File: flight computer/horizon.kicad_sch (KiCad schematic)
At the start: 37 parts, among them J2 Conn_02x03_Counter_Clockwise, J7 Conn_02x03_Counter_Clockwise, J8 Conn_02x03_Counter_Clockwise, U1 MMCU, U3 NMCU, U4 TMCU, Y1 Crystal

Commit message: Ummm, more baro routing to the MCU and stuff
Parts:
- removed R28: R, Resistor_SMD:R_0603_1608Metric, symbol Device:R
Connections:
- net SCK TMCU: now reaches U4.18 (PA09)
- net CS TMCU: no longer names the net of U4.17 (PA08)
- no-connect marks 82 -> 81
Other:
- note added: "Pull low to talk"
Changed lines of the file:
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@@
 		)
 	)
+	(text "Pull low to talk"
+		(exclude_from_sim no)
+		(at 187.706 49.784 0)
+		(effects
+			(font
+				(size 1.27 1.27)
+			)
+		)
+	)
 	(text "GPS → MCU RX"
 		(exclude_from_sim no)
@@
 	)
 	(junction
-		(at 176.53 49.53)
-		(diameter 0)
-		(color 0 0 0 0)
-	)
-	(junction
 		(at 52.07 30.48)
 		(diameter 0)
@@
 	)
 	(no_connect
-		(at 127 67.31)
-	)
-	(no_connect
 		(at 31.75 86.36)
 	)
@@
 	(wire
 		(pts
-			(xy 176.53 49.53) (xy 162.56 49.53)
-		)
-		(stroke
-			(width 0)
-			(type default)
-		)
-	)
-	(wire
-		(pts
 			(xy 46.99 31.75) (xy 52.07 31.75)
 		)
@@
 	(wire
 		(pts
-			(xy 177.8 49.53) (xy 176.53 49.53)
-		)
-		(stroke
-			(width 0)
-			(type default)
-		)
-	)
-	(wire
-		(pts
 			(xy 147.32 35.56) (xy 147.32 36.83)
 		)
@@
 	(global_label "CS_BARO TMCU"
 		(shape input)
-		(at 177.8 49.53 0)
+		(at 162.56 49.53 0)
 		(fields_autoplaced yes)
 		(effects
@@
 		)
 		(property "Intersheetrefs" "${INTERSHEET_REFS}"
-			(at 195.1785 49.53 0)
+			(at 179.9385 49.53 0)
 			(effects
 				(font
@@
 		)
 	)
+	(global_label "SCK TMCU"
+		(shape input)
+		(at 127 67.31 180)
+		(fields_autoplaced yes)
+		(effects
+			(font
+				(size 1.27 1.27)
+			)
+			(justify right)
+		)
+		(property "Intersheetrefs" "${INTERSHEET_REFS}"
+			(at 114.2782 67.31 0)
+			(effects
+				(font
+					(size 1.27 1.27)
+				)
+				(justify right)
+				(hide yes)
+			)
+		)
+	)
 	(global_label "TX TMCU"
 		(shape input)
@@
 		)
 	)
-	(global_label "CS TMCU"
-		(shape input)
-		(at 127 64.77 180)
-		(fields_autoplaced yes)
-		(effects
-			(font
-				(size 1.27 1.27)
-			)
-			(justify right)
-		)
-		(property "Intersheetrefs" "${INTERSHEET_REFS}"
-			(at 115.5482 64.77 0)
-			(effects
-				(font
-					(size 1.27 1.27)
-				)
-				(justify right)
-				(hide yes)
-			)
-		)
-	)
 	(global_label "I2C0_SDA"
 		(shape input)
@@
 	)
 	(symbol
-		(lib_id "Device:R")
-		(at 176.53 53.34 0)
-		(unit 1)
-		(exclude_from_sim no)
-		(in_bom yes)
-		(on_board yes)
-		(dnp no)
-		(property "Reference" "R28"
-			(at 171.196 53.594 0)
-			(effects
-				(font
-					(size 1.27 1.27)
-				)
-				(justify left)
-			)
-		)
-		(property "Value" "R"
-			(at 171.196 56.134 0)
-			(effects
-				(font
-					(size 1.27 1.27)
-				)
-				(justify left)
-			)
-		)
-		(property "Footprint" "Resistor_SMD:R_0603_1608Metric"
-			(at 174.752 53.34 90)
-			(effects
-				(font
-					(size 1.27 1.27)
-				)
-				(hide yes)
-			)
-		)
-		(property "Datasheet" "~"
-			(at 176.53 53.34 0)
-			(effects
-				(font
-					(size 1.27 1.27)
-				)
-				(hide yes)
-			)
-		)
-		(property "Description" "Resistor"
-			(at 176.53 53.34 0)
-			(effects
-				(font
-					(size 1.27 1.27)
-				)
-				(hide yes)
-			)
-		)
-		(pin "2"
-		)
-		(pin "1"
-		)
-		(instances
-			(project "horizon"
-				(path "/78d9c2f3-deae-418a-8c21-4820ea8fc57f"
-					(reference "R28")
-					(unit 1)
-				)
-			)
-		)
-	)
-	(symbol
 		(lib_id "power:+3.3V")
 		(at 45.72 143.51 270)
@@
 					(unit 1)
 				)
-			)
-		)
-	)
-	(symbol
-		(lib_id "power:+3.3V")
-		(at 176.53 57.15 180)
-		(unit 1)
-		(exclude_from_sim no)
-		(in_bom yes)
-		(on_board yes)
-		(dnp no)
-		(property "Reference" "#PWR097"
-			(at 176.53 53.34 0)
-			(effects
-				(font
-					(size 1.27 1.27)
-				)
-				(hide yes)
-			)
-		)
-		(property "Value" "+3.3V"
-			(at 176.53 62.484 90)
-			(effects
-				(font
-					(size 1.27 1.27)
-				)
-			)
-		)
-		(property "Footprint" ""
-			(at 176.53 57.15 0)
-			(effects
-				(font
-					(size 1.27 1.27)
-				)
-				(hide yes)
-			)
-		)
-		(property "Datasheet" ""
-			(at 176.53 57.15 0)
-			(effects
-				(font
-					(size 1.27 1.27)
-				)
-				(hide yes)
-			)
-		)
-		(property "Description" "Power symbol creates a global label with name \"+3.3V\""
-			(at 176.53 57.15 0)
-			(effects
-				(font
-					(size 1.27 1.27)
-				)
-				(hide yes)
-			)
-		)
-		(pin "1"
-		)
-		(instances
-			(project "horizon"
-				(path "/78d9c2f3-deae-418a-8c21-4820ea8fc57f"
-					(reference "#PWR097")
-					(unit 1)
-				)

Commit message: wiring almost done
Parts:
- Y1: footprint Crystal:Crystal_SMD_0603-2Pin_6.0x3.5mm -> Crystal:Crystal_AT310_D3.0mm_L10.0mm_Vertical
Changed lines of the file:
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@@
 			)
 		)
-		(property "Footprint" "Crystal:Crystal_SMD_0603-2Pin_6.0x3.5mm"
+		(property "Footprint" "Crystal:Crystal_AT310_D3.0mm_L10.0mm_Vertical"
 			(at 279.4 91.44 0)
 			(effects

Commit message: for you scooter <3
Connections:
- net GND: now also J2.4 (Pin_4), J7.4 (Pin_4), J8.4 (Pin_4)
- net SWCLK DMCU-1: now also J7.6 (Pin_6); no longer J7.2 (Pin_2)
- net SWCLK DMCU-2: now also J8.6 (Pin_6); no longer J8.2 (Pin_2)
- net SWCLK MMCU: now also J2.6 (Pin_6); no longer J2.2 (Pin_2)
- net SWDIO DMCU-1: now also J7.2 (Pin_2); no longer J7.5 (Pin_5)
- net SWDIO DMCU-2: now also J8.2 (Pin_2); no longer J8.5 (Pin_5)
- net SWDIO MMCU: now also J2.2 (Pin_2); no longer J2.5 (Pin_5)
- net nRESET DMCU-1: now also J7.5 (Pin_5); no longer J7.4 (Pin_4)
- net nRESET DMCU-2: now also J8.5 (Pin_5); no longer J8.4 (Pin_4)
- net nRESET MMCU: now also J2.5 (Pin_5); no longer J2.4 (Pin_4)
- no-connect marks 81 -> 78
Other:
- moved on the sheet: C10, C17, C63, C64, C65, C66, C67, J2, J7, J8, R29, R3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

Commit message: idk, changes
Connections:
- net mosfet3_signalfire: no longer names the net of U3.30 (PA13)
- no-connect marks 78 -> 79
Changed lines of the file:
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@@
+	)
+	(no_connect
+		(at 31.75 73.66)
 	)
 	(no_connect
@@
 			(effects
 				(font
-					(size 1.27 1.27)
-				)
-				(justify right)
-				(hide yes)
-			)
-		)
-	)
-	(global_label "mosfet3_signalfire"
-		(shape input)
-		(at 31.75 73.66 180)
-		(fields_autoplaced yes)
-		(effects
-			(font
-				(size 1.27 1.27)
-			)
-			(justify right)
-		)
-		(property "Intersheetrefs" "${INTERSHEET_REFS}"
-			(at 11.2269 73.66 0)
-			(effects
-				(font

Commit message: drc
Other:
- moved on the sheet: C10, C17, C63, C64, C65, C66, C67, J2, R29, R30, R4, R6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

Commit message: Started wiring the teensy bootloader
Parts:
- added U2: MKL02Z32VFG4, Package_DFN_QFN:QFN-16-1EP_3x3mm_P0.5mm_EP1.9x1.9mm, symbol MCU_NXP_Kinetis:MKL02Z32VFG4
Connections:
- net +3.3V: now also U2.1 (VDD/VREFH)
- net GND: now also U2.2 (VSS/VREFL)
- net PTA2: now reaches U1.24 (PTA2)
- net PTA2: now also U2.9 (PTB1/IRQ_6)
- net PTA3: now reaches U1.25 (PTA3)
- net PTA3: now also U2.7 (PTA7/IRQ_4)
- no-connect marks 79 -> 77

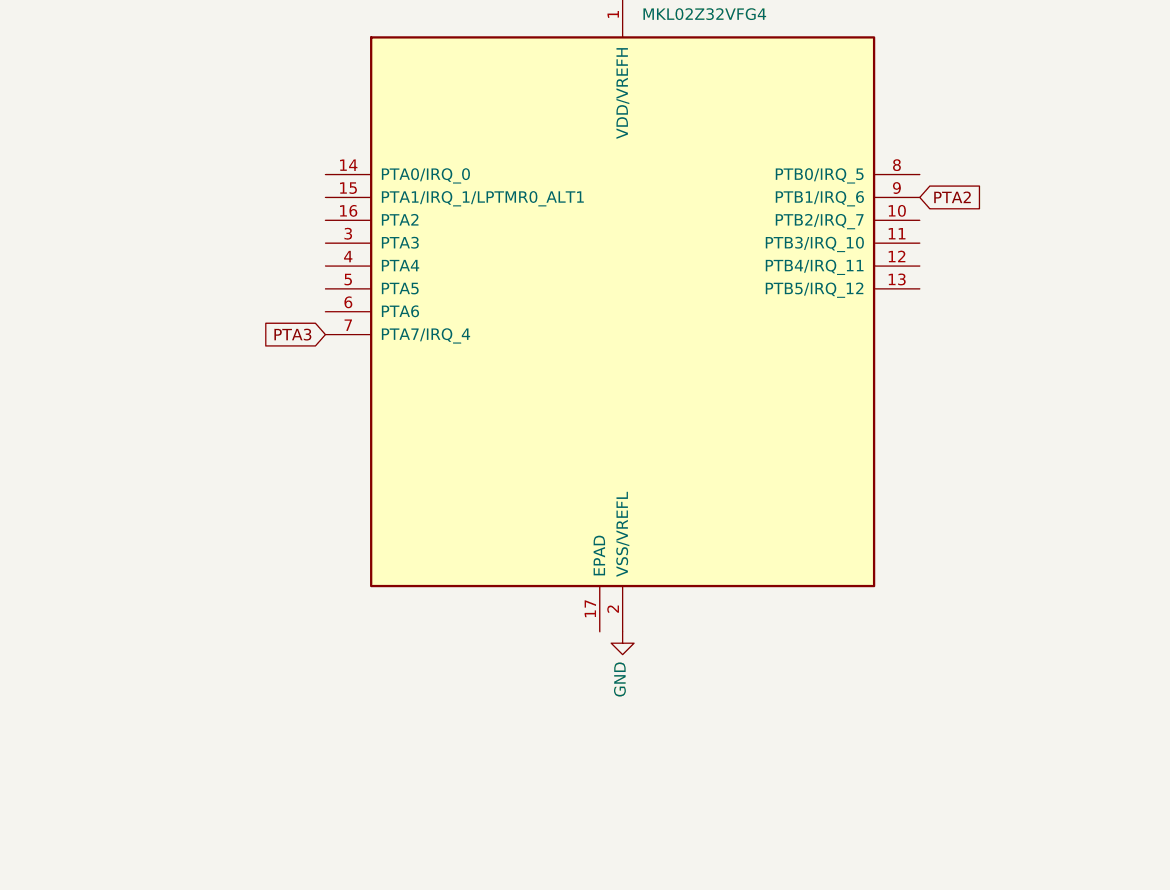
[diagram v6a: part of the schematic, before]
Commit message: Finished wiring the teensy bootloader
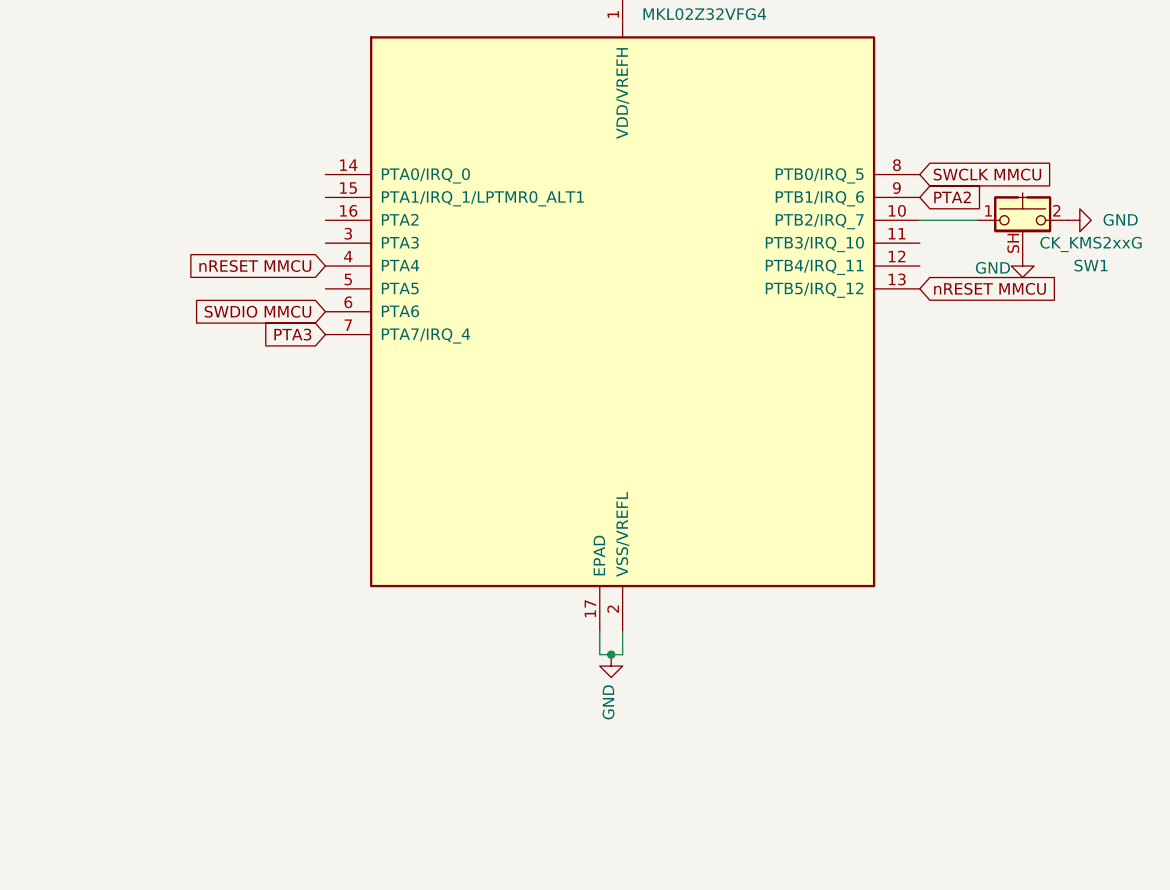
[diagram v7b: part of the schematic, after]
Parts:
- added SW1: CK_KMS2xxG, Button_Switch_SMD:SW_SPST_CK_KMS2xxGP, symbol Switch:CK_KMS2xxG
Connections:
- net GND: now also U2.17 (EPAD), SW1.2, SW1.SH (B)
- net SWCLK MMCU: now also U2.8 (PTB0/IRQ_5)
- net SWDIO MMCU: now also U2.6 (PTA6)
- net nRESET MMCU: now also U2.13 (PTB5/IRQ_12), U2.4 (PTA4)
- net at U2.10 (PTB2/IRQ_7): now also SW1.1

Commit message: a few small changes to make cyao happy!
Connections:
- net 1R: now also U1.50 (D13/SCK/LED); no longer U1.28 (D3/CAN-TX/PWM)
- net SWCLK DMCU-1: now also U3.58 (PA31); no longer U3.57 (PA30)
- net SWDIO DMCU-1: now also U3.57 (PA30); no longer U3.58 (PA31)
- net mosfet1_signal: now also U4.27 (PB14); no longer U3.14 (PA05)
- net mosfet2_signal: now also U4.26 (PB13); no longer U3.15 (PA06)
- net mosfet3_signal: now also U4.25 (PB12); no longer U3.16 (PA07)
- no-connect marks 77 -> 73
